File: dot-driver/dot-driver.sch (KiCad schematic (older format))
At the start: 56 parts, among them J1 5VL, J10 Conn_01x03_Male, J11 Conn_01x03_Male, J12 Conn_01x03_Male, J13 Conn_01x03_Male, J14 Micro_SD_Card_Det_Hirose_DM3AT, J15 SWD, J2 5VL, J3 GND, J4 GND, J5 USB_B_Micro, J6 Conn_01x03_Male, J7 Conn_01x03_Male, J8 Conn_01x03_Male, J9 Conn_01x03_Male, SW1 BUTTON, U1 AP2127N-3.3, U2 STM32F105RCTx, Y1 12MHz

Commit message: start working on output ability
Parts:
- Y1: value 12MHz -> 8MHz
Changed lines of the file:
@@
 P 3450 3600
 F 0 "Y1" V 3404 3731 50  0000 L CNN
-F 1 "12MHz" V 3495 3731 50  0000 L CNN
+F 1 "8MHz" V 3495 3731 50  0000 L CNN
 F 2 "Crystals:Crystal_SMD_5032_4Pads" H 3450 3600 50  0001 C CNN
 F 3 "~" H 3450 3600 50  0001 C CNN

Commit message: Improve schematic and layout, but they are out of sync
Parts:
- removed D1, D2: D, Diodes_SMD:SOD-323, symbol Device:D
- removed D6: GREEN, LEDs:LED_0603, symbol Device:LED
- removed R1, R11, R13, R15, R17, R3, R6, R9: 1K, Resistors_SMD:R_0603, symbol Device:R
- removed R10, R12, R14, R16, R18, R2, R4, R8: 470R, Resistors_SMD:R_0603, symbol Device:R
- removed R7: 680R, Resistors_SMD:R_0603, symbol Device:R
- added J?: External button, symbol Connector:Conn_01x02_Male
- added Q?: SSM3J338R, symbol Device:Q_PMOS_GSD
- added RN?: 480R, Resistor_THT:R_Array_SIP9, symbol Device:R_Network08
- added RN?: 1K, Resistor_THT:R_Array_SIP9, symbol Device:R_Network08
- J1, J2: value 5VL -> 5V
- J14: symbol Connector:Micro_SD_Card_Det_Hirose_DM3AT -> dot-driver-rescue:Micro_SD_Card_Det_Hirose_DM3AT-Connector
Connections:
- net labels removed: +5VL, VDD
- wire segments 111 -> 138
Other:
- moved on the sheet: C1, C2, D10, D11, D3, D4, D5, D7, D8, D9, J1, J10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

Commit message: Route rev2 of driver board
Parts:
- J5: renamed from J?; footprint (none) -> Pin_Headers:Pin_Header_Straight_1x02
- Q1: renamed from Q?; footprint (none) -> TO_SOT_Packages_SMD:SOT-23
- RN1, RN2: renamed from RN?; footprint Resistor_THT:R_Array_SIP9 -> Resistors_SMD:R_Array_Convex_5x0603
- renumbered C5 to C3, C6 to C4, C3 to C5, C4 to C6, D3 to D1, D4 to D2, D5 to D3, D7 to D4, D12 to D5, D8 to D6, D9 to D7, D10 to D8, D11 to D9, J6 to J1, J13 to J10, J1 to J11, J2 to J12, J3 to J13, J4 to J14, J14 to J15, J15 to J16, J5 to J2, J7 to J3, J8 to J4, J9 to J6, J10 to J7, J11 to J8, J12 to J9, R5 to R1, R19 to R2
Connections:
- net labels added: INDCAT0, INDCAT1, INDCAT2, INDCAT3, INDCAT4, INDCAT5, INDCAT6, INDCAT7
- wire segments 138 -> 133
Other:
- moved on the sheet: RN1

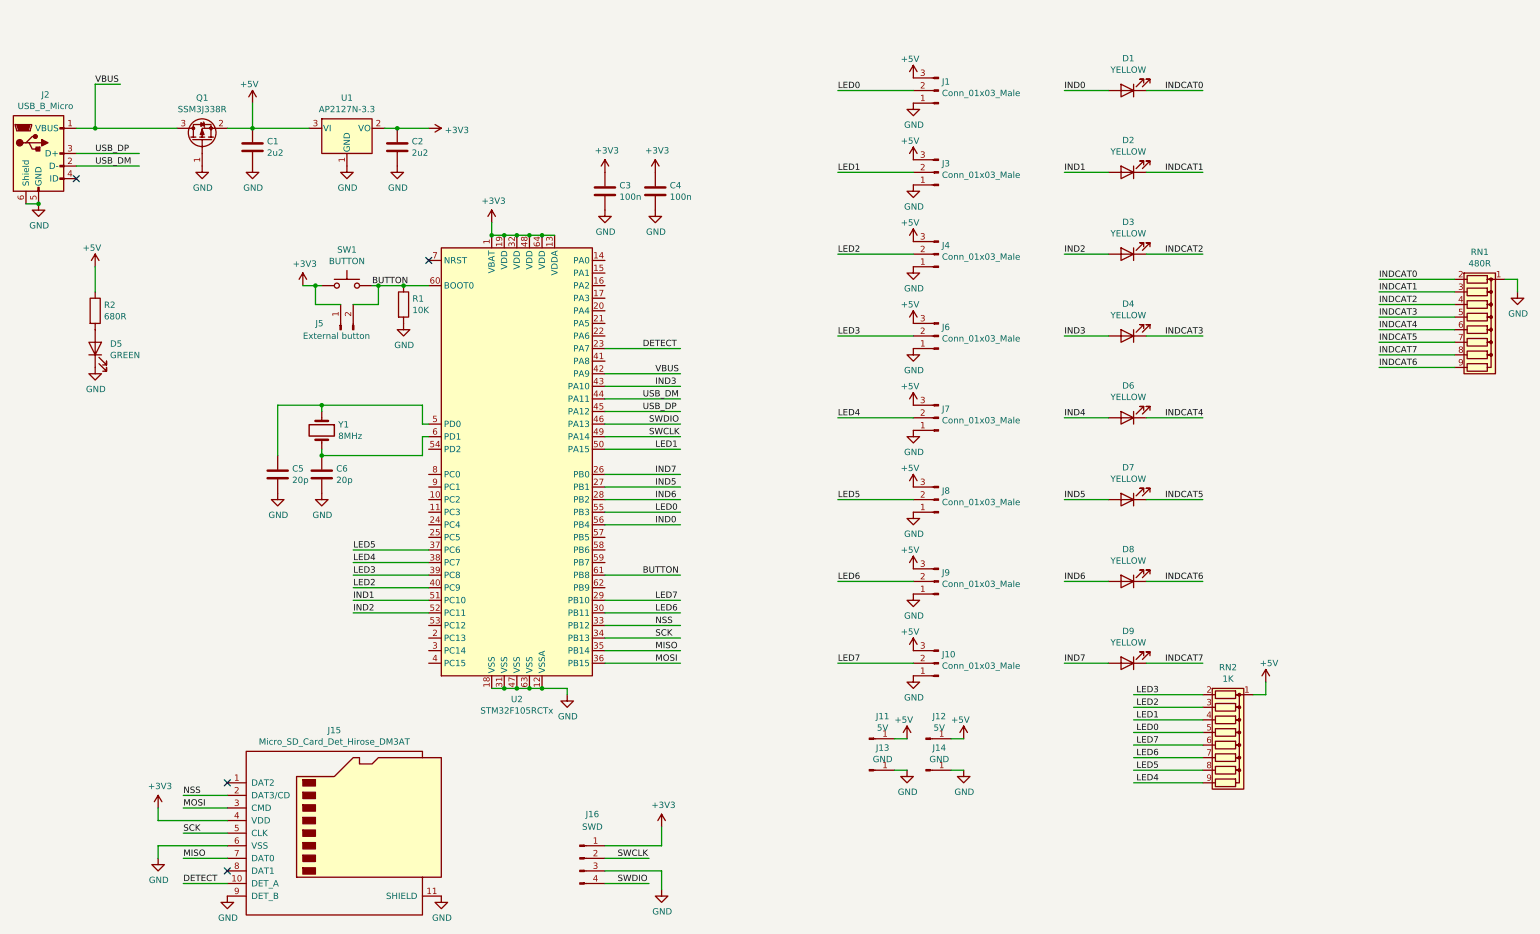
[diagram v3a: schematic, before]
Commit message: Begin work on static pattern for firefly
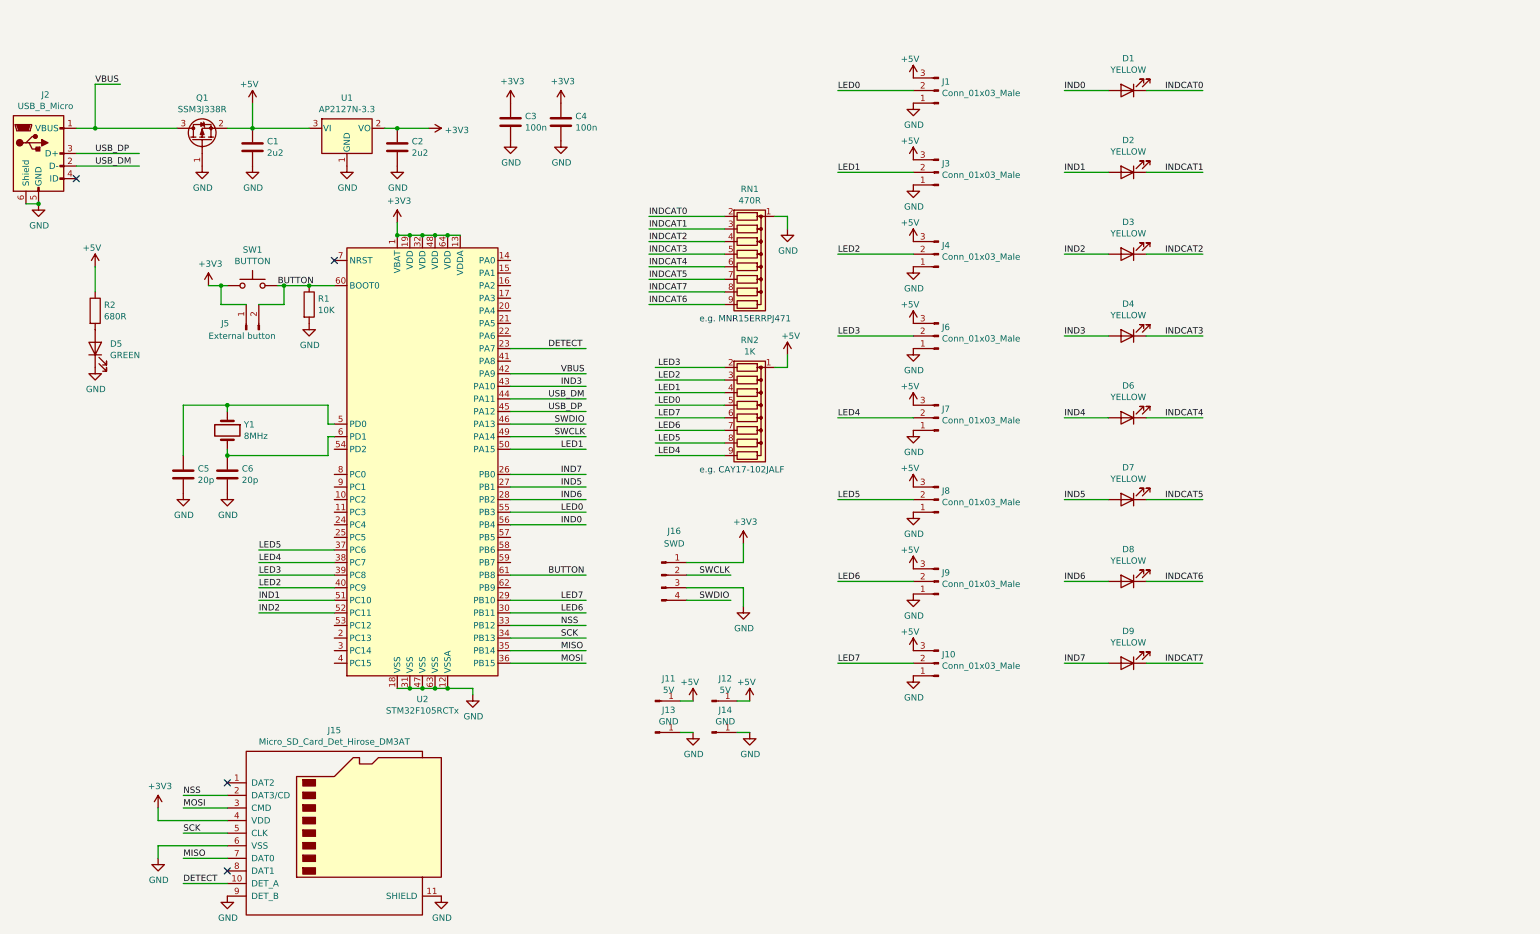
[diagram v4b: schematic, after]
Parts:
- RN1: value 480R -> 470R
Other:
- note added: "e.g. CAY17-102JALF"
- note added: "e.g. MNR15ERRPJ471"
- moved on the sheet: C3, C4, C5, C6, J11, J12, J13, J14, J16, J5, R1, RN1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
